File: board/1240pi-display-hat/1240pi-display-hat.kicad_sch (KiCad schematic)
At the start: 7 parts, among them J1 Conn_02x05_Odd_Even

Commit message: Split hats into separate projects / boards.
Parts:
- P208: footprint Package_DIP:DIP-14_W7.62mm -> (none)
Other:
- title: 1240-Pi Modification Boards -> 1240-Pi Display Board Mod
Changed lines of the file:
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@@
   (paper "USLetter")
   (title_block
-    (title "1240-Pi Modification Boards")
+    (title "1240-Pi Display Board Mod")
     (date "2022-04-21")
     (rev "1.0")
@@
       (effects (font (size 1.27 1.27)) (justify left))
     )
-    (property "Footprint" "Package_DIP:DIP-14_W7.62mm" (id 2) (at 22.86 170.18 0)
+    (property "Footprint" "" (id 2) (at 22.86 170.18 0)
       (effects (font (size 1.27 1.27)) hide)
     )
@@
     (property "Reference" "P208" (id 0) (at 251.46 165.1 0))
     (property "Value" "" (id 1) (at 251.46 167.64 0))
-    (property "Footprint" "Package_DIP:DIP-14_W7.62mm" (id 2) (at 251.46 173.99 0)
+    (property "Footprint" "" (id 2) (at 251.46 173.99 0)
       (effects (font (size 1.27 1.27)) hide)
     )
@@
     (property "Reference" "P208" (id 0) (at 251.46 132.08 0))
     (property "Value" "" (id 1) (at 251.46 134.62 0))
-    (property "Footprint" "Package_DIP:DIP-14_W7.62mm" (id 2) (at 251.46 140.97 0)
+    (property "Footprint" "" (id 2) (at 251.46 140.97 0)
       (effects (font (size 1.27 1.27)) hide)
     )
@@
       (effects (font (size 1.27 1.27)) hide)
     )
-    (property "Value" "" (id 1) (at 33.02 144.78 0))
+    (property "Value" "~" (id 1) (at 33.02 144.78 0))
     (property "Footprint" "" (id 2) (at 33.02 149.86 0)
       (effects (font (size 1.27 1.27)) hide)
@@
       (effects (font (size 1.27 1.27)) hide)
     )
-    (property "Value" "" (id 1) (at 33.02 195.58 0))
+    (property "Value" "~" (id 1) (at 33.02 195.58 0))
     (property "Footprint" "" (id 2) (at 33.02 190.5 0)
       (effects (font (size 1.27 1.27)) hide)
@@
     (property "Reference" "P208" (id 0) (at 251.46 99.06 0))
     (property "Value" "" (id 1) (at 251.46 101.6 0))
-    (property "Footprint" "Package_DIP:DIP-14_W7.62mm" (id 2) (at 251.46 107.95 0)
+    (property "Footprint" "" (id 2) (at 251.46 107.95 0)
       (effects (font (size 1.27 1.27)) hide)
     )
@@
     (property "Reference" "P208" (id 0) (at 73.66 110.49 0))
     (property "Value" "" (id 1) (at 73.66 113.03 0))
-    (property "Footprint" "Package_DIP:DIP-14_W7.62mm" (id 2) (at 73.66 118.11 0)
+    (property "Footprint" "" (id 2) (at 73.66 118.11 0)
       (effects (font (size 1.27 1.27)) hide)
     )
@@
     (property "Reference" "P208" (id 0) (at 251.46 66.04 0))
     (property "Value" "" (id 1) (at 251.46 68.58 0))
-    (property "Footprint" "Package_DIP:DIP-14_W7.62mm" (id 2) (at 251.46 74.93 0)
+    (property "Footprint" "" (id 2) (at 251.46 74.93 0)
       (effects (font (size 1.27 1.27)) hide)
     )
@@
     (property "Reference" "P208" (id 0) (at 251.46 33.02 0))
     (property "Value" "" (id 1) (at 251.46 35.56 0))
-    (property "Footprint" "Package_DIP:DIP-14_W7.62mm" (id 2) (at 251.46 41.91 0)
+    (property "Footprint" "" (id 2) (at 251.46 41.91 0)
       (effects (font (size 1.27 1.27)) hide)
     )
@@
     (pin "7")
   )
+  (sheet_instances
+    (path "/" (page "1"))
+  )
+  (symbol_instances
+    (path "/42c270aa-ca51-44e2-a7e1-5b3c2a82720f"
+      (reference "#FLG0101") (unit 1) (value "~") (footprint "")
+    )
+    (path "/3702cd3c-879c-4c20-9276-eeaab458842a"
+      (reference "#FLG0102") (unit 1) (value "~") (footprint "")
+    )
+    (path "/33dc1d17-3c43-484e-a994-57309880e165"
+      (reference "#PWR0101") (unit 1) (value "GND") (footprint "")
+    )
+    (path "/29b6733f-e2ce-499b-a093-b144f7ab4e51"
+      (reference "#PWR0102") (unit 1) (value "+5V") (footprint "")
+    )
+    (path "/c489f835-fda8-4917-bdf1-fb025402198e"
+      (reference "#PWR0103") (unit 1) (value "+5V") (footprint "")
+    )
+    (path "/81f7c4ec-a1ba-4df2-9d04-990fde4df218"
+      (reference "#PWR0104") (unit 1) (value "GND") (footprint "")
+    )
+    (path "/80a0843d-8e1d-4eab-9068-32674a47fe97"
+      (reference "#PWR0105") (unit 1) (value "GND") (footprint "")
+    )
+    (path "/75a11c0c-9043-4723-93bf-97178f7d2b90"
+      (reference "J1") (unit 1) (value "Conn_02x05_Odd_Even") (footprint "Connector_PinHeader_2.54mm:PinHeader_2x05_P2.54mm_Vertical")
+    )
+    (path "/fc642cd8-7c35-4e61-a3f8-93bdddadf08c"
+      (reference "P208") (unit 1) (value "Header") (footprint "Package_DIP:DIP-14_W7.62mm")
+    )
+    (path "/d6d8f6e8-8ce2-4bfa-a4ce-1ad33f5433ef"
+      (reference "P208") (unit 2) (value "Header") (footprint "Package_DIP:DIP-14_W7.62mm")
+    )
+    (path "/1515e87a-84d7-4cbb-979b-ed34e71c4b3d"
+      (reference "P208") (unit 3) (value "Header") (footprint "Package_DIP:DIP-14_W7.62mm")
+    )
+    (path "/4da2da3e-3334-444a-831d-d4a3a6e9f58f"
+      (reference "P208") (unit 4) (value "Header") (footprint "Package_DIP:DIP-14_W7.62mm")
+    )
+    (path "/2a886ba3-86f4-4d5f-a754-dbda2fbf9643"
+      (reference "P208") (unit 5) (value "Header") (footprint "Package_DIP:DIP-14_W7.62mm")
+    )
+    (path "/6dbb9fa6-8855-4c67-961d-cb5dab718fa7"
+      (reference "P208") (unit 6) (value "Header") (footprint "Package_DIP:DIP-14_W7.62mm")
+    )
+    (path "/132a5e0b-6c8d-4520-993e-55bde96dc44f"
+      (reference "P208") (unit 7) (value "Header") (footprint "Package_DIP:DIP-14_W7.62mm")
+    )
+    (path "/c4cc4576-5c3f-48b7-b12d-d7ef5a85b073"
+      (reference "P415") (unit 1) (value "Header") (footprint "Package_DIP:DIP-14_W7.62mm")
+    )
+    (path "/5863b5cc-1809-4a29-9f24-007ee9486c34"
+      (reference "P415") (unit 2) (value "Header") (footprint "Package_DIP:DIP-14_W7.62mm")
+    )
+    (path "/39c70d9c-b85f-4aab-b4a8-2cffd6c147e7"
+      (reference "P415") (unit 3) (value "Header") (footprint "Package_DIP:DIP-14_W7.62mm")
+    )
+    (path "/b91e8f31-48aa-4060-962c-f4d34479a4e2"
+      (reference "R1") (unit 1) (value "10k") (footprint "Resistor_THT:R_Axial_DIN0207_L6.3mm_D2.5mm_P10.16mm_Horizontal")
+    )
+    (path "/e66d8f6f-aa8b-48d8-bb2b-bde00dc24d64"
+      (reference "U1") (unit 1) (value "74F126") (footprint "Package_DIP:DIP-14_W7.62mm")
+    )
+    (path "/ce51fc0a-4f8f-4d4f-913f-78fb93f99c89"
+      (reference "U1") (unit 2) (value "74F126") (footprint "Package_DIP:DIP-14_W7.62mm")
+    )
+    (path "/b4a11166-d330-4bf6-972c-79ef30a58405"
+      (reference "U1") (unit 3) (value "74F126") (footprint "Package_DIP:DIP-14_W7.62mm")
+    )
+    (path "/977427f6-7f40-4ace-b36e-af6819e8bcc3"
+      (reference "U1") (unit 4) (value "74F126") (footprint "Package_DIP:DIP-14_W7.62mm")
+    )
+    (path "/6f10aa5a-83f3-444d-87f8-603ad7d62493"
+      (reference "U1") (unit 5) (value "74F126") (footprint "Package_DIP:DIP-14_W7.62mm")
+    )
+    (path "/b7cfe9de-6558-4664-81e0-75eb115c6f77"
+      (reference "U208") (unit 1) (value "74F04") (footprint "Package_DIP:DIP-14_W7.62mm")
+    )
+    (path "/6dd15017-af57-4398-a4e6-e46969184433"
+      (reference "U208") (unit 2) (value "74F04") (footprint "Package_DIP:DIP-14_W7.62mm")
+    )
+    (path "/5973b297-5c9e-42b1-b43b-91699dc9bd68"
+      (reference "U208") (unit 3) (value "74F04") (footprint "Package_DIP:DIP-14_W7.62mm")
+    )
+    (path "/61948ac7-7ba3-46c6-8b79-aff5a868c2a6"
+      (reference "U208") (unit 4) (value "74F04") (footprint "Package_DIP:DIP-14_W7.62mm")
+    )
+    (path "/06ebc70e-0b3e-4883-a3b6-63466eb95a8b"
+      (reference "U208") (unit 5) (value "74F04") (footprint "Package_DIP:DIP-14_W7.62mm")
+    )
+    (path "/796ac916-f633-438b-b727-05869855ee39"
+      (reference "U208") (unit 6) (value "74F04") (footprint "Package_DIP:DIP-14_W7.62mm")
+    )
+    (path "/ee20cff8-9076-4d71-9010-6d3a4a592e6c"
+      (reference "U208") (unit 7) (value "74F04") (footprint "Package_DIP:DIP-14_W7.62mm")
+    )
+    (path "/940bfab3-cd6f-4f64-8731-c072194350a7"
+      (reference "U415") (unit 1) (value "74S74") (footprint "Package_DIP:DIP-14_W7.62mm")
+    )
+    (path "/bc15e106-ffe1-4d77-8e64-6edabb56b25e"
+      (reference "U415") (unit 2) (value "74S74") (footprint "Package_DIP:DIP-14_W7.62mm")
+    )
+    (path "/42f494a0-47c8-45e5-8a63-e37ff542165c"
+      (reference "U415") (unit 3) (value "74S74") (footprint "Package_DIP:DIP-14_W7.62mm")
+    )
+  )
 )

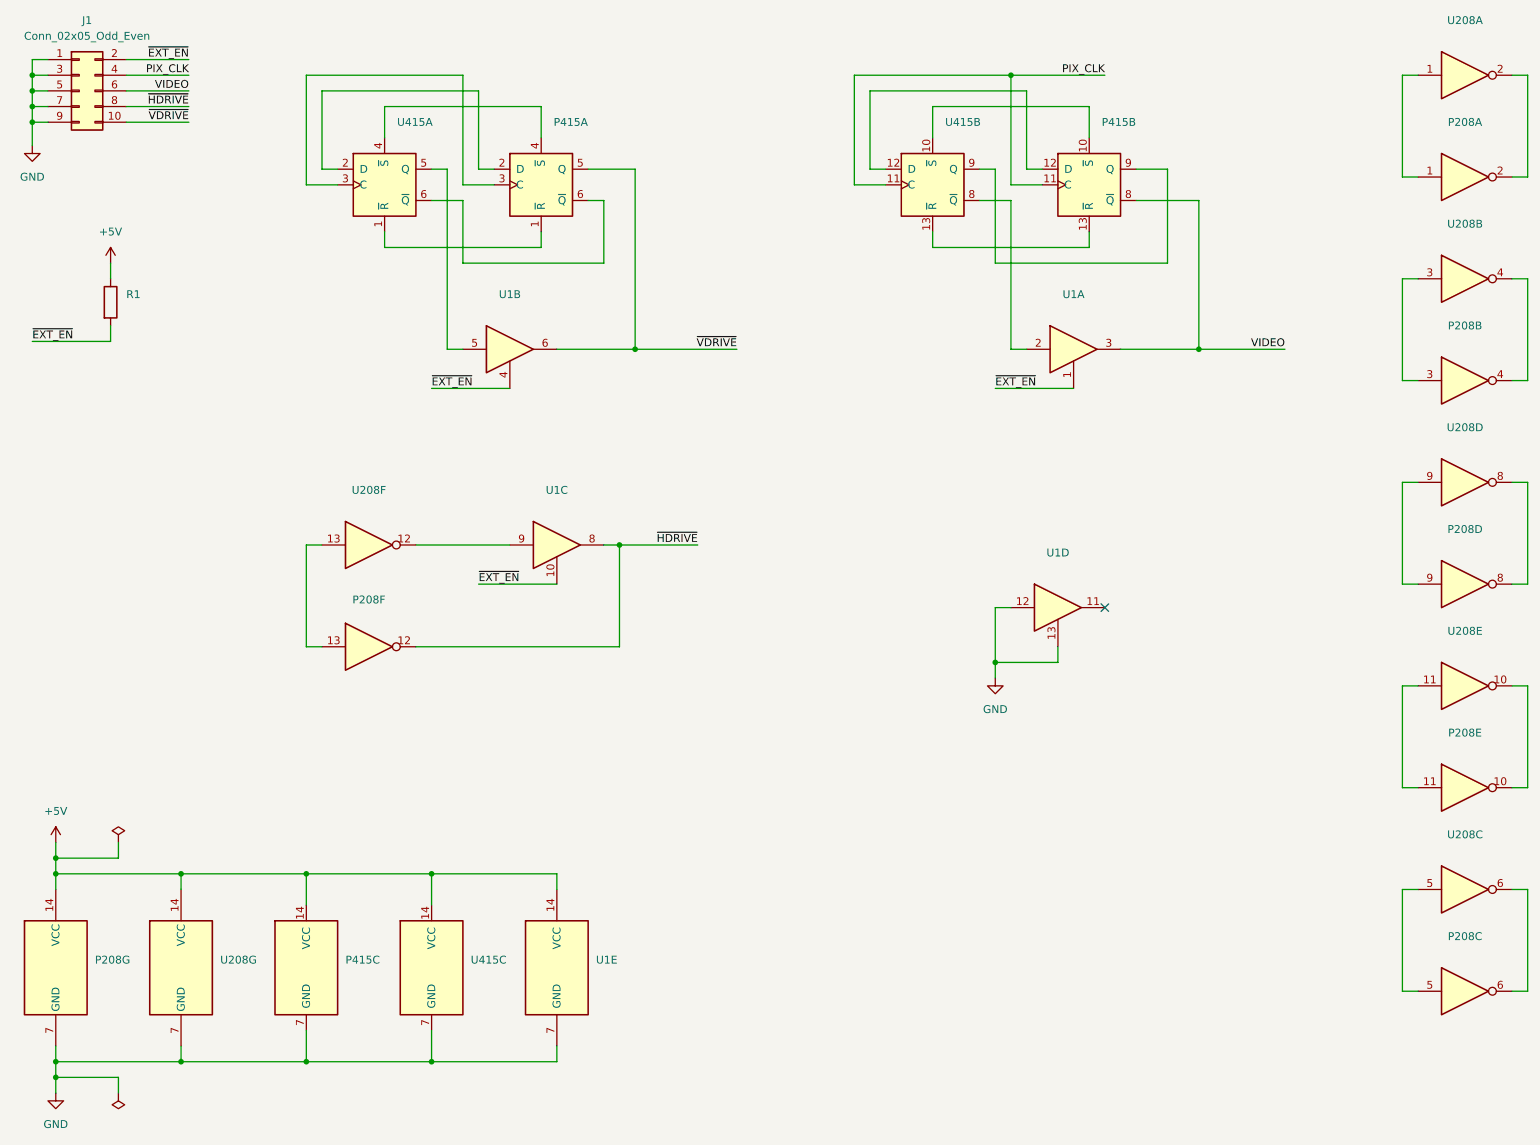
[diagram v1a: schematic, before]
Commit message: Switch hat boards from IDC ribbons to flat flex cables.
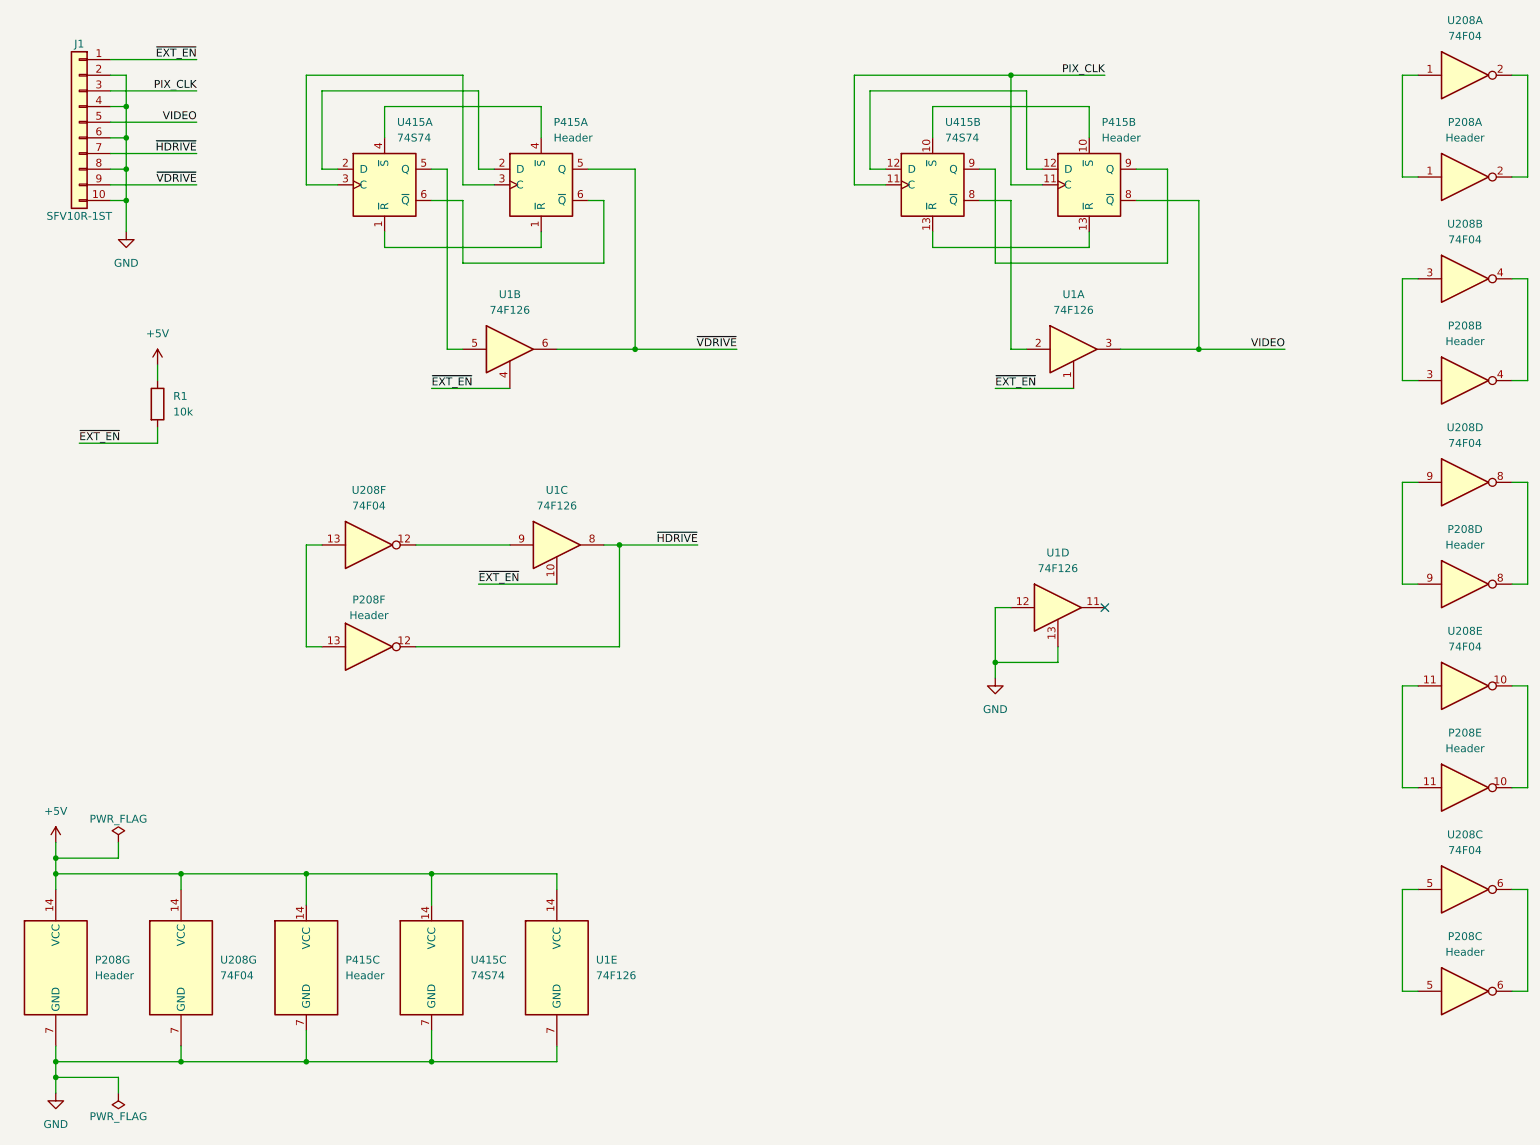
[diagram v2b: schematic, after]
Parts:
- removed J1: Conn_02x05_Odd_Even, Connector_PinHeader_2.54mm:PinHeader_2x05_P2.54mm_Vertical, symbol Connector_Generic:Conn_02x05_Odd_Even
- added J1: SFV10R-1ST, 0Local:Amphenol_SFV10R-1ST, symbol Connector_Generic:Conn_01x10
- P208: value (none) -> Header; footprint (none) -> Package_DIP:DIP-14_W7.62mm
- P415: value (none) -> Header
- R1: value (none) -> 10k; footprint (none) -> Resistor_THT:R_Axial_DIN0207_L6.3mm_D2.5mm_P10.16mm_Horizontal
- U1: value (none) -> 74F126; footprint (none) -> Package_DIP:DIP-14_W7.62mm
- U208: value (none) -> 74F04; footprint (none) -> Package_DIP:DIP-14_W7.62mm
- U415: value (none) -> 74S74; footprint (none) -> Package_DIP:DIP-14_W7.62mm
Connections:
- net GND: now also J1.10 (Pin_10), J1.2 (Pin_2), J1.4 (Pin_4), J1.6 (Pin_6), J1.8 (Pin_8)
- net PIX_CLK: now also J1.3 (Pin_3)
- net VIDEO: now also J1.5 (Pin_5)
- net ~{EXT_EN}: now also J1.1 (Pin_1)
- net ~{HDRIVE}: now also J1.7 (Pin_7)
- net ~{VDRIVE}: now also J1.9 (Pin_9)
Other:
- company: © 2022 Sam Hanes, licensed under CERN-OHL-P v2 -> © 2022 Sam Hanes, licensed under CERN-OHL-S v2
- moved on the sheet: R1

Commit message: Update board license to CERN-OHL-S v2+.
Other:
- company: © 2022 Sam Hanes, licensed under CERN-OHL-S v2 -> © 2022 Sam Hanes, licensed under CERN-OHL-S v2+
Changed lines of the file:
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@@
     (date "2022-05-21")
     (rev "1.0")
-    (company "© 2022 Sam Hanes, licensed under CERN-OHL-S v2")
+    (company "© 2022 Sam Hanes, licensed under CERN-OHL-S v2+")
     (comment 1 "https://github.com/Elemecca/1240pi")
   )
